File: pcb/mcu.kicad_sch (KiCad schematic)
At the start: 23 parts, among them J1 TC2030, SW1 GSPTS0018, SW2 GSPTS0018, U1 STM32H730VBTx, Y1 ECS-160-12-33B2Q-JES-TR3

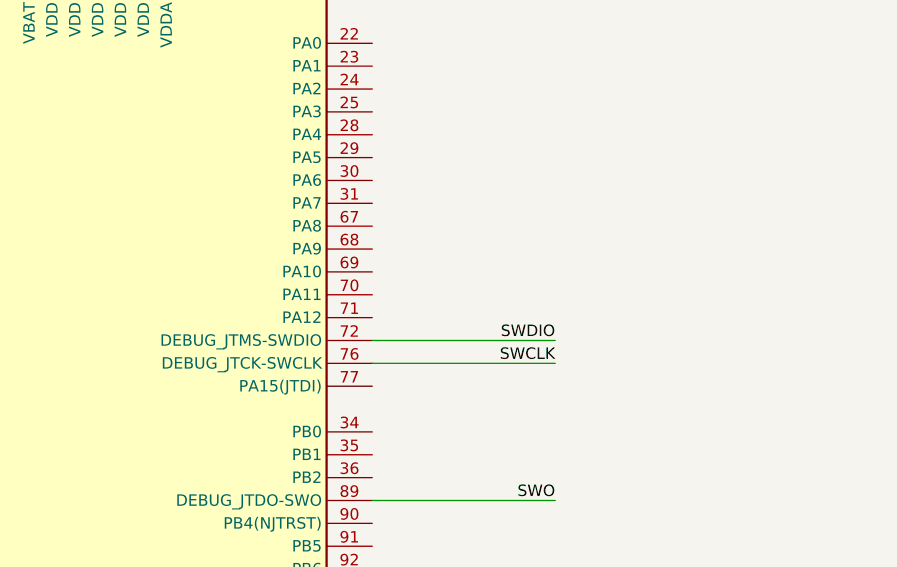
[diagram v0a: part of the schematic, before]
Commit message: Add USB
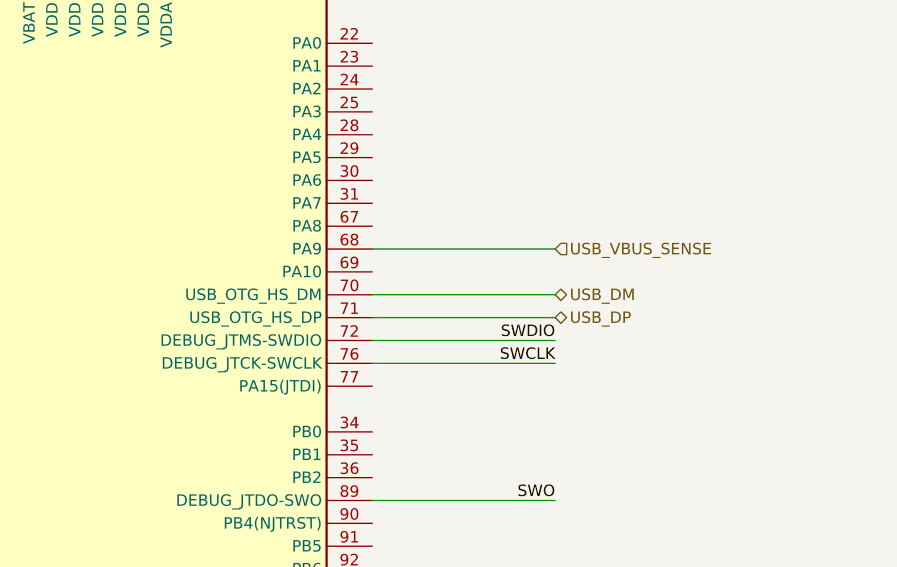
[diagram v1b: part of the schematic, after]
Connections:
- net USB_VBUS_SENSE: now reaches U1.68 (PA9)
- net USB_DM: now reaches U1.70 (PA11)
- net USB_DP: now reaches U1.71 (PA12)

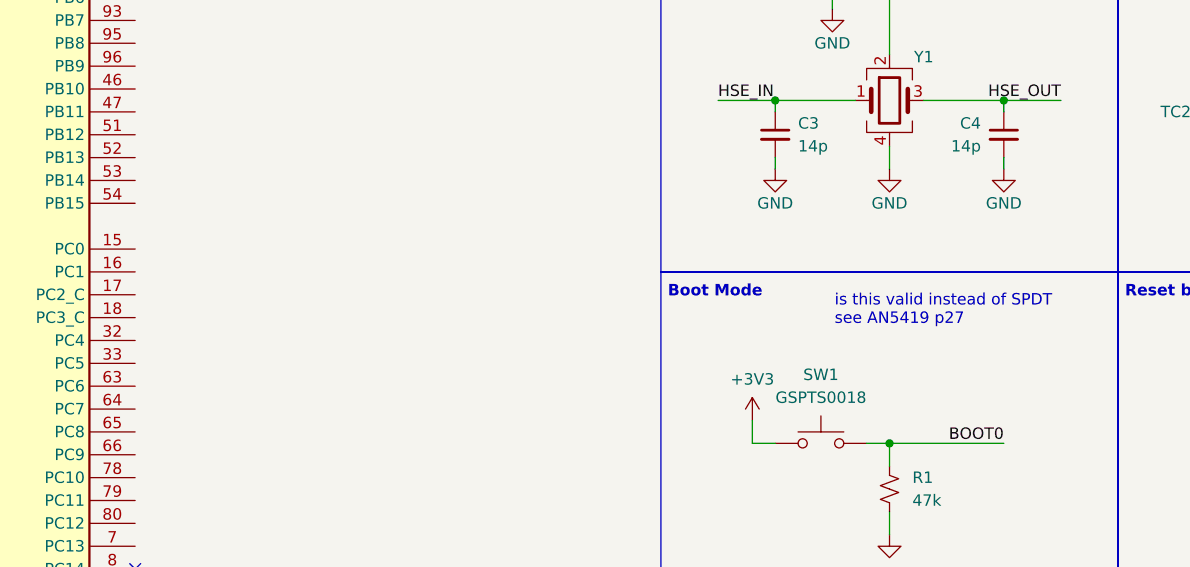
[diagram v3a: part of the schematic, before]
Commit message: Implement flash memory connection
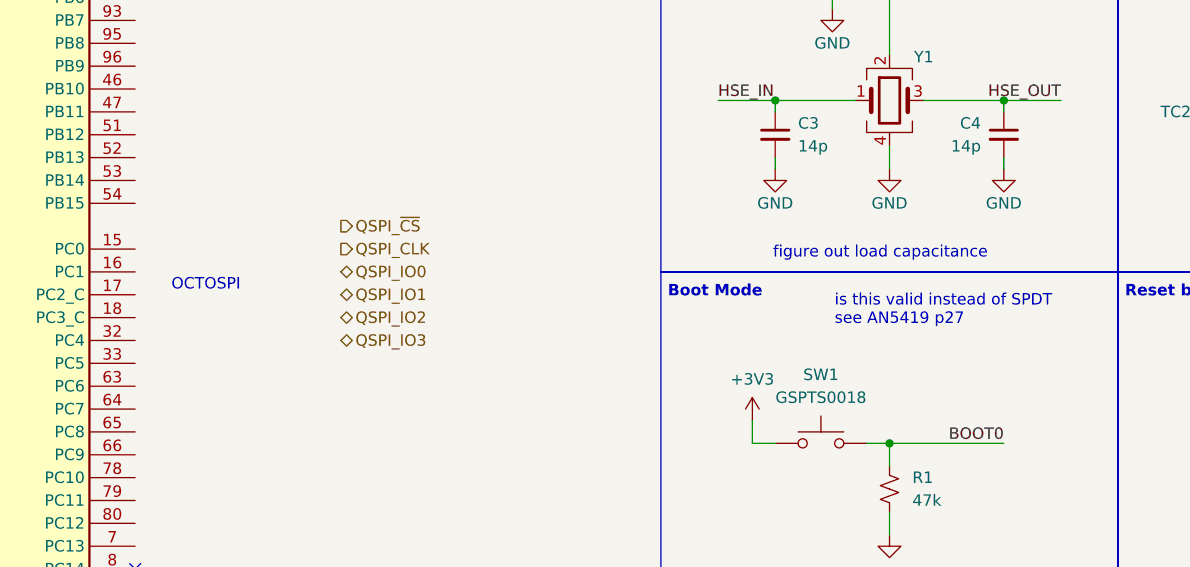
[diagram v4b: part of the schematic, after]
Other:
- note added: "OCTOSPI"
- note added: "figure out load capacitance"

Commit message: Add sensors sheet
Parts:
- removed J1: TC2030, Connector:Tag-Connect_TC2030-IDC-FP_2x03_P1.27mm_Vertical, symbol Connector:Conn_ARM_SWD_TagConnect_TC2030
- C15: now not fitted
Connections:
- net SERVO_SIG: now reaches U1.22 (PA0)
- net SERVO_EN: now reaches U1.23 (PA1)
- net DEBUG_JTDI: now reaches U1.77 (PA15(JTDI))
- net VCP_TX: now reaches U1.78 (PC10)
- net VCP_RX: now reaches U1.79 (PC11)
- net SWCLK renamed DEBUG_JTCK-SWCLK
- net SWDIO renamed DEBUG_JTMS-SWDIO
- net SWO renamed DEBUG_JTDO-SWO
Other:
- note added: "debatable if needed internal pullup"
- note removed: "Debug"
